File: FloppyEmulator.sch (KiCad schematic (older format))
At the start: 1 part

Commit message: Bit of update
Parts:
- added Q1: Crystal_GND24, symbol Crystal_GND24
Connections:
- net SPI2_MISO: no longer U?.52 (PC11/ADC1_EXTI11/ADC2_EXTI11/ADC3_EXTI11/I2S3_ext_SD/SDIO_D3/SPI3_MISO/UART4_RX/USART3_RX)
- net SPI2_MOSI: no longer U?.53 (PC12/I2S3_SD/SDIO_CK/SPI3_MOSI/UART5_TX/USART3_CK)
- net SPI2_SCK: no longer U?.51 (PC10/I2S3_CK/SDIO_D2/SPI3_SCK/UART4_TX/USART3_TX)
- net GND: now reaches U?.12 (VSSA)
- net GND: now also U?.18 (VSS), U?.63 (VSS)
- net +3V3: now reaches U?.13 (VDDA)
- net +3V3: now also U?.19 (VDD), U?.32 (VDD), U?.48 (VDD), U?.64 (VDD)
- net at U?.5 (PH0/RCC_OSC_IN): now also Q1.3
- net at U?.6 (PH1/RCC_OSC_OUT): now also Q1.1
- net SCL: now reaches U?.61 (CAN1_RX/I2C1_SCL/SDIO_D4/TIM10_CH1/TIM4_CH3/PB8)
- net SDA: now reaches U?.62 (CAN1_TX/DAC_EXTI9/I2C1_SDA/I2S2_WS/SDIO_D5/SPI2_NSS/TIM11_CH1/TIM4_CH4/PB9)
- new net SPI3_MISO: U?.52 (PC11/ADC1_EXTI11/ADC2_EXTI11/ADC3_EXTI11/I2S3_ext_SD/SDIO_D3/SPI3_MISO/UART4_RX/USART3_RX)
- new net SPI3_MOSI: U?.53 (PC12/I2S3_SD/SDIO_CK/SPI3_MOSI/UART5_TX/USART3_CK)
- new net SPI3_SCK: U?.51 (PC10/I2S3_CK/SDIO_D2/SPI3_SCK/UART4_TX/USART3_TX)
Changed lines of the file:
@@
 U 1 1 5A44968C
 P 8575 5200
-F 0 "U?" H 8575 3114 50  0000 C CNN
-F 1 "STM32F405RGTx" H 8575 3023 50  0000 C CNN
+F 0 "U?" H 8575 2925 50  0000 C CNN
+F 1 "STM32F405RGTx" H 8575 2800 50  0000 C CNN
 F 2 "LQFP64" H 12775 7075 50  0001 R TNN
 F 3 "" H 8575 5200 50  0001 C CNN
@@
 	12875 5100 13100 5100
 Text GLabel 4000 6300 0    50   Output ~ 0
-SPI2_SCK
+SPI3_SCK
 Text GLabel 4000 6400 0    50   Input ~ 0
-SPI2_MISO
+SPI3_MISO
 Text GLabel 4000 6500 0    50   Output ~ 0
-SPI2_MOSI
+SPI3_MOSI
 Wire Wire Line
 	4275 6300 4000 6300
@@
 Text Notes 5800 2625 0    60   ~ 0
 2 ??? Disk Change Detect on Shugart Interface or Density Select on IBM PC\n4 ???\n6 ??? Can be Drive Select 3 on Amiga\n8 <-- Index\n10 --> Motor Enable A\n12 --> Drive Select B\n14 --> Drive Select A\n16 --> Motor Enable B\n18 --> Step\n20 --> Dir\n22 --> Write Data\n24 --> Write Enable\n26 <-- Track 00\n28 <-- Write Protect\n30 <-- Read Data\n32 --> Side / Head\n34 <-- Disk Change / Ready
+$Comp
+L Crystal_GND24 Q1
+U 1 1 5A44A2C6
+P 3725 4850
+F 0 "Q1" V 3775 5425 50  0000 R CNN
+F 1 "Crystal_GND24" V 3700 5825 50  0000 R CNN
+F 2 "" H 3725 4850 50  0001 C CNN
+F 3 "" H 3725 4850 50  0001 C CNN
+	1    3725 4850
+	0    -1   -1   0
+$EndComp
+Wire Wire Line
+	3725 4700 3725 4550
+Wire Wire Line
+	3725 4550 4075 4550
+Wire Wire Line
+	4075 4550 4075 4800
+Wire Wire Line
+	4075 4800 4275 4800
+Wire Wire Line
+	4275 4900 4075 4900
+Wire Wire Line
+	4075 4900 4075 5125
+Wire Wire Line
+	4075 5125 3725 5125
+Wire Wire Line
+	3725 5125 3725 5000
+Text GLabel 1825 7825 0    60   Input ~ 0
++5VDC
+Text GLabel 1825 8125 0    60   Input ~ 0
+GND
+$Comp
+L GND #PWR?
+U 1 1 5A44A7FF
+P 1925 8275
+F 0 "#PWR?" H 1925 8025 50  0001 C CNN
+F 1 "GND" H 1930 8102 50  0001 C CNN
+F 2 "" H 1925 8275 50  0001 C CNN
+F 3 "" H 1925 8275 50  0001 C CNN
+	1    1925 8275
+	1    0    0    -1
+$EndComp
+Wire Wire Line
+	1925 8275 1925 8125
+Wire Wire Line
+	1925 8125 1825 8125
+Wire Wire Line
+	1825 7825 2100 7825
+$Comp
+L GND #PWR?
+U 1 1 5A44A98F
+P 8475 7200
+F 0 "#PWR?" H 8475 6950 50  0001 C CNN
+F 1 "GND" H 8480 7027 50  0001 C CNN
+F 2 "" H 8475 7200 50  0001 C CNN
+F 3 "" H 8475 7200 50  0001 C CNN
+	1    8475 7200
+	1    0    0    -1
+$EndComp
+$Comp
+L GND #PWR?
+U 1 1 5A44A9D8
+P 8575 7200
+F 0 "#PWR?" H 8575 6950 50  0001 C CNN
+F 1 "GND" H 8580 7027 50  0001 C CNN
+F 2 "" H 8575 7200 50  0001 C CNN
+F 3 "" H 8575 7200 50  0001 C CNN
+	1    8575 7200
+	1    0    0    -1
+$EndComp
+$Comp
+L GND #PWR?
+U 1 1 5A44A9E7
+P 8675 7200
+F 0 "#PWR?" H 8675 6950 50  0001 C CNN
+F 1 "GND" H 8680 7027 50  0001 C CNN
+F 2 "" H 8675 7200 50  0001 C CNN
+F 3 "" H 8675 7200 50  0001 C CNN
+	1    8675 7200
+	1    0    0    -1
+$EndComp
+Wire Wire Line
+	8375 3200 8375 3050
+Wire Wire Line
+	8375 3050 8775 3050
+Wire Wire Line
+	8775 3050 8775 3200
+Wire Wire Line
+	8675 3200 8675 3050
+Connection ~ 8675 3050
+Wire Wire Line
+	8575 2825 8575 3200
+Connection ~ 8575 3050
+Wire Wire Line
+	8475 3200 8475 3050
+Connection ~ 8475 3050
+Wire Wire Line
+	8575 2825 8750 2825
+Text GLabel 8750 2825 2    60   Input ~ 0
++3V3
+Wire Wire Line
+	12875 6100 13100 6100
+Wire Wire Line
+	12875 6200 13100 6200
+Text GLabel 13100 6100 2    50   Output ~ 0
+SCL
+Text GLabel 13100 6200 2    50   BiDi ~ 0
+SDA
 $EndSCHEMATC

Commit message: Signals assigned
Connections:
- net WRGATE: now reaches U?.10 (PC2/ADC1_IN12/ADC2_IN12/ADC3_IN12/I2S2_ext_SD/SPI2_MISO/USB_OTG_HS_ULPI_DIR)
- net WRDATA: now reaches U?.11 (PC3/ADC1_IN13/ADC2_IN13/ADC3_IN13/I2S2_SD/SPI2_MOSI/USB_OTG_HS_ULPI_NXT)
- net SEL0: now reaches U?.14 (ADC1_IN0/ADC2_IN0/ADC3_IN0/SYS_WKUP/TIM2_CH1/TIM2_ETR/TIM5_CH1/TIM8_ETR/UART4_TX/USART2_CTS/PA0)
- net SEL1: now reaches U?.15 (ADC1_IN1/ADC2_IN1/ADC3_IN1/TIM2_CH2/TIM5_CH2/UART4_RX/USART2_RTS/PA1)
- net SEL2: now reaches U?.16 (ADC1_IN2/ADC2_IN2/ADC3_IN2/TIM2_CH3/TIM5_CH3/TIM9_CH1/USART2_TX/PA2)
- net SEL3: now reaches U?.17 (ADC1_IN3/ADC2_IN3/ADC3_IN3/TIM2_CH4/TIM5_CH4/TIM9_CH2/USART2_RX/USB_OTG_HS_ULPI_D0/PA3)
- net INDEX: now reaches U?.2 (PC13/ANTI_TAMP/RTC_AF1)
- net TRACK0: now reaches U?.3 (PC14/RCC_OSC32_IN)
- net WPROT: now reaches U?.4 (PC15/ADC1_EXTI15/ADC2_EXTI15/ADC3_EXTI15/RCC_OSC32_OUT)
- net BEEP: now reaches U?.41 (I2C3_SCL/RCC_MCO_1/TIM1_CH1/USART1_CK/USB_OTG_FS_SOF/PA8)
- net LCD_DC: now reaches U?.54 (PD2/SDIO_CMD/TIM3_ETR/UART5_RX)
- net LCD_RESET: now reaches U?.55 (I2S3_CK/SPI1_SCK/SPI3_SCK/SYS_JTDO-SWO/TIM2_CH2/PB3)
- net BUTTON1: now reaches U?.56 (I2S3_ext_SD/SPI1_MISO/SPI3_MISO/SYS_JTRST/TIM3_CH1/PB4)
- net BUTTON2: now reaches U?.57 (CAN2_RX/I2C1_SMBA/I2S3_SD/SPI1_MOSI/SPI3_MOSI/TIM3_CH2/USB_OTG_HS_ULPI_D7/PB5)
- net BUTTON3: now reaches U?.58 (CAN2_TX/I2C1_SCL/TIM4_CH1/USART1_TX/PB6)
- net BUTTON4: now reaches U?.59 (I2C1_SDA/TIM4_CH2/USART1_RX/PB7)
- net SIDE: now reaches U?.8 (PC0/ADC1_IN10/ADC2_IN10/ADC3_IN10/USB_OTG_HS_ULPI_STP)
- net STEP: now reaches U?.9 (PC1/ADC1_IN11/ADC2_IN11/ADC3_IN11)
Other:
- note added: "BUTTONS, LED(s) and BEEPER"
- note added: "LCD"
- note added: "MFM Flow"
- note added: "OUTPUT SIGNALS:\n\n- Index\n- Track 0\n- Write Protect\n- Read Data\n- Disk Change/Ready\n- Reserved ???"
- note removed: "OUTPUT SIGNALS:\n\n- Index\n- Track 0\n- Write Protect\n- Read Data\n- Disk Change/Ready"
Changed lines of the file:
@@
 INPUT SIGNALS:\n\n- Drive Select 0\n- Drive Select 1\n- Motor Enable A\n- Motor Enable B\n- Dir\n- Side (INTERRUPT)\n- Step (INTERRUPT)\n- Write Gate (INTERRUPT)\n- Write Data (INTERRUPT)\n- Reserved ?
 Text Notes 3575 1650 0    60   ~ 0
-OUTPUT SIGNALS:\n\n- Index\n- Track 0\n- Write Protect\n- Read Data\n- Disk Change/Ready
+OUTPUT SIGNALS:\n\n- Index\n- Track 0\n- Write Protect\n- Read Data\n- Disk Change/Ready\n- Reserved ???
 Text Notes 1175 3025 0    60   ~ 0
 Amiga Drive ID readout:\n\n- turn Select off\n- turn Motor on and off\n- pulse Select and read ID bits on Ready line
@@
 	4275 4900 4075 4900
 Wire Wire Line
-	4075 4900 4075 5125
+	4075 4900 4075 5025
 Wire Wire Line
-	4075 5125 3725 5125
+	4075 5025 3725 5025
 Wire Wire Line
-	3725 5125 3725 5000
+	3725 5025 3725 5000
 Text GLabel 1825 7825 0    60   Input ~ 0
 +5VDC
@@
 Text GLabel 13100 6200 2    50   BiDi ~ 0
 SDA
+Text Notes 850  3825 0    60   ~ 0
+BUTTONS, LED(s) and BEEPER
+Text Notes 13700 6675 0    60   ~ 0
+MFM Flow
+Text Notes 3325 6450 0    60   ~ 0
+LCD
+Wire Wire Line
+	4275 5100 3125 5100
+Text Label 3125 5100 0    60   ~ 0
+LCD_DC
+Wire Wire Line
+	12875 5600 13650 5600
+Text Label 13650 5600 2    60   ~ 0
+LCD_RESET
+Wire Wire Line
+	12875 5700 13650 5700
+Wire Wire Line
+	12875 5800 13650 5800
+Wire Wire Line
+	12875 5900 13650 5900
+Wire Wire Line
+	12875 6000 13650 6000
+Text Label 13650 5700 2    60   ~ 0
+BUTTON1
+Text Label 13650 5800 2    60   ~ 0
+BUTTON2
+Text Label 13650 5900 2    60   ~ 0
+BUTTON3
+Text Label 13650 6000 2    60   ~ 0
+BUTTON4
+Wire Wire Line
+	4275 6600 2900 6600
+Wire Wire Line
+	4275 6700 2900 6700
+Wire Wire Line
+	4275 6800 2900 6800
+Text Label 2900 6600 0    60   ~ 0
+INDEX
+Text Label 2900 6700 0    60   ~ 0
+TRACK0
+Text Label 2900 6800 0    60   ~ 0
+WPROT
+Wire Wire Line
+	4275 5300 2900 5300
+Wire Wire Line
+	4275 5400 2900 5400
+Wire Wire Line
+	4275 5500 2900 5500
+Text Label 2900 5300 0    60   ~ 0
+SIDE
+Text Label 2900 5400 0    60   ~ 0
+STEP
+Text Label 2900 5500 0    60   ~ 0
+WRGATE
+Wire Wire Line
+	4275 5600 2900 5600
+Text Label 2900 5600 0    60   ~ 0
+WRDATA
+Wire Wire Line
+	12875 3600 13600 3600
+Wire Wire Line
+	12875 3700 13600 3700
+Wire Wire Line
+	12875 3800 13600 3800
+Wire Wire Line
+	12875 3900 13600 3900
+Text Label 13600 3600 2    60   ~ 0
+SEL0
+Text Label 13600 3700 2    60   ~ 0
+SEL1
+Text Label 13600 3800 2    60   ~ 0
+SEL2
+Text Label 13600 3900 2    60   ~ 0
+SEL3
+Wire Wire Line
+	12875 4400 13100 4400
+Text GLabel 13100 4400 2    50   Output ~ 0
+BEEP
 $EndSCHEMATC

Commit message: Draft components placement
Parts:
- added X1: Micro_SD_Card_Det, symbol Micro_SD_Card_Det
- added X2: Conn_01x09, components:QVGA_LCD_9pin, symbol Conn_01x09
- added X3: Conn_02x17_Odd_Even, Pin_Headers:Pin_Header_Straight_2x17_Pitch2.54mm, symbol Conn_02x17_Odd_Even
- added X4: Conn_01x04, Pin_Headers:Pin_Header_Angled_1x04_Pitch2.54mm, symbol Conn_01x04
- U1: renamed from U?; footprint LQFP64 -> Housings_QFP:LQFP-64_10x10mm_Pitch0.5mm
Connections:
- net +3V3: now also X2.1 (Pin_1)
- net GND: now also X1.11 (SHIELD), X1.6 (VSS), X1.9 (DET_B), X2.2 (Pin_2)
- net LCD_DC: now also X2.5 (Pin_5)
- net LCD_RESET: now also X2.4 (Pin_4)
- net SPI3_MISO: now also X2.9 (Pin_9)
- net SPI3_MOSI: now also X2.6 (Pin_6)
- net SPI3_NSS: now also X2.3 (Pin_3)
- net SPI3_SCK: now also X2.7 (Pin_7)
- new net BACKLIGHT: X2.8 (Pin_8)
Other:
- note added: "microSD connector:\nMOLEX 5027740891"
- note removed: "SD Card"

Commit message: Add microSD footprint. Update schematic and PCB
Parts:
- added U2, U3, U4, U5, U? (x2): SN74LVC2G07, TO_SOT_Packages_SMD:SOT-23-6, symbol SN74LVC2G07
- X1: footprint (none) -> components:MOLEX_5027740891
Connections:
- net labels added: CARD_DETECT, DIR
- wire segments 63 -> 113
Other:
- note added: "5-way SMD Joystick ALPS SKRHABE010"
- note added: "ESD?\nPull-ups?"
- note added: "MOLEX 5027740891"
- note added: "SN74LV1T34 Logic Buffer Translator\nSN74LVC2G07 Dual Open Drain Buffer"
- note added: "use open drain"
- note removed: "microSD connector:\nMOLEX 5027740891"
- moved on the sheet: X1, X3, X4

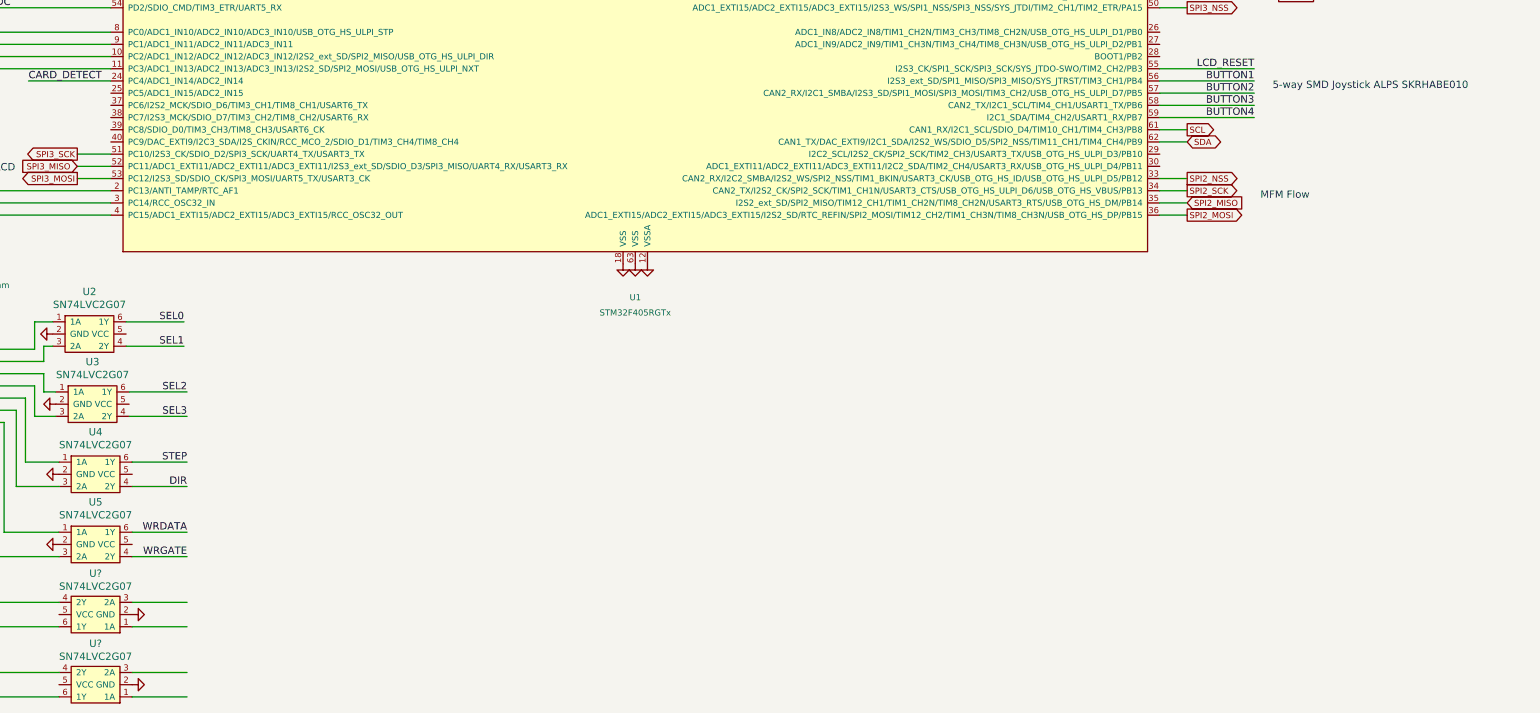
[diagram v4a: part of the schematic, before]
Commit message: Add ALPS 5-way joystick
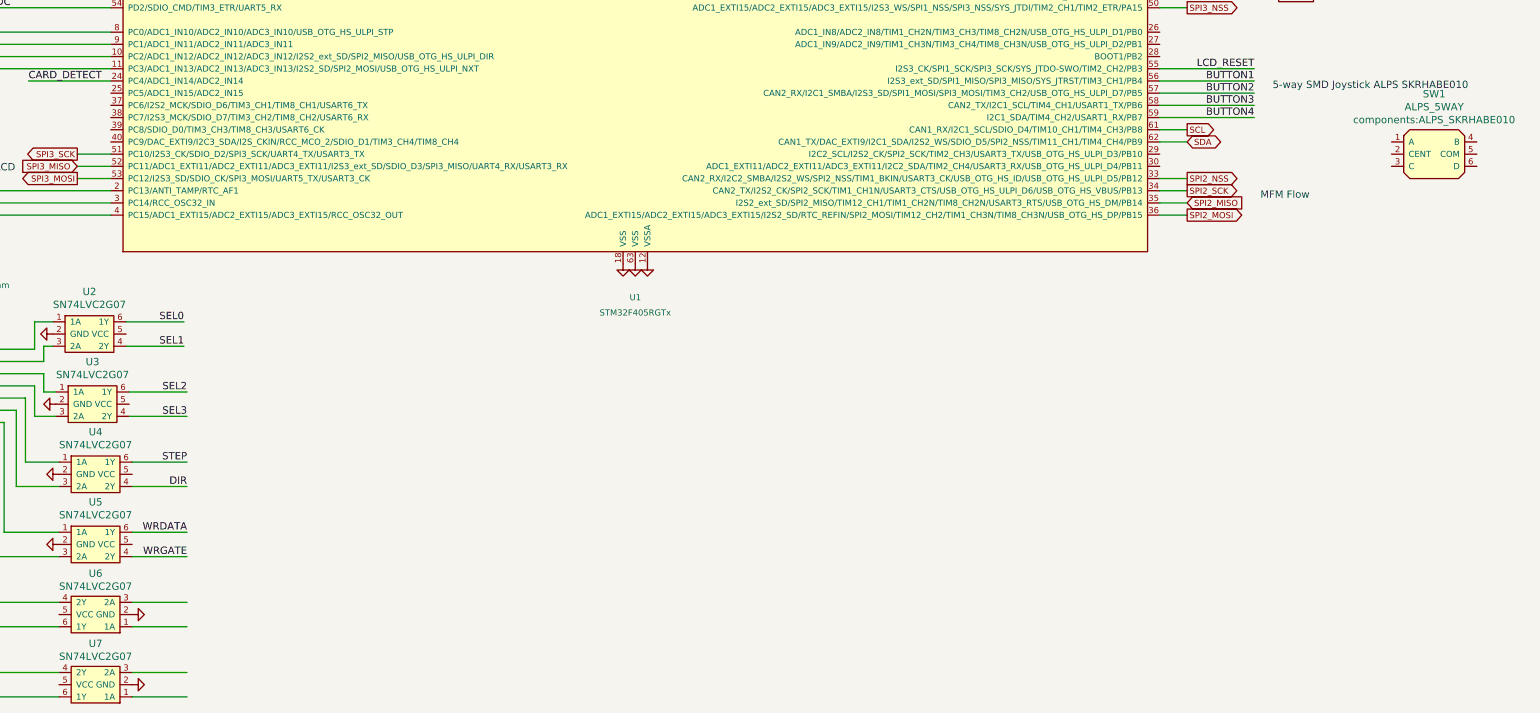
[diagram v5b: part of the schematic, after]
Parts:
- added SW1: ALPS_5WAY, components:ALPS_SKRHABE010, symbol ALPS_5WAY
- gave numbers to parts that had none: 2
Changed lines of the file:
@@
 WRDATA
 $Comp
-L SN74LVC2G07 U?
+L SN74LVC2G07 U6
 U 1 1 5A453572
 P 4150 10075
-F 0 "U?" H 4150 9738 60  0000 C CNN
+F 0 "U6" H 4150 9738 60  0000 C CNN
 F 1 "SN74LVC2G07" H 4150 9844 60  0000 C CNN
 F 2 "TO_SOT_Packages_SMD:SOT-23-6" H 4150 10325 60  0001 C CNN
@@
 $EndComp
 $Comp
-L SN74LVC2G07 U?
+L SN74LVC2G07 U7
 U 1 1 5A4535E1
 P 4150 10650
-F 0 "U?" H 4150 10313 60  0000 C CNN
+F 0 "U7" H 4150 10313 60  0000 C CNN
 F 1 "SN74LVC2G07" H 4150 10419 60  0000 C CNN
 F 2 "TO_SOT_Packages_SMD:SOT-23-6" H 4150 10900 60  0001 C CNN
@@
 	2900 10750 3850 10750
 $Comp
-L GND #PWR?
+L GND #PWR013
 U 1 1 5A4538FF
 P 4450 10075
-F 0 "#PWR?" H 4450 9825 50  0001 C CNN
+F 0 "#PWR013" H 4450 9825 50  0001 C CNN
 F 1 "GND" H 4455 9902 50  0001 C CNN
 F 2 "" H 4450 10075 50  0001 C CNN
@@
 $EndComp
 $Comp
-L GND #PWR?
+L GND #PWR014
 U 1 1 5A45393A
 P 4450 10650
-F 0 "#PWR?" H 4450 10400 50  0001 C CNN
+F 0 "#PWR014" H 4450 10400 50  0001 C CNN
 F 1 "GND" H 4455 10477 50  0001 C CNN
 F 2 "" H 4450 10650 50  0001 C CNN
@@
 Text Notes 13800 5775 0    60   ~ 0
 5-way SMD Joystick ALPS SKRHABE010
+$Comp
+L ALPS_5WAY SW1
+U 1 1 5A4545D4
+P 15125 6300
+F 0 "SW1" H 15125 6793 60  0000 C CNN
+F 1 "ALPS_5WAY" H 15125 6687 60  0000 C CNN
+F 2 "components:ALPS_SKRHABE010" H 15125 6581 60  0000 C CNN
+F 3 "" H 15125 6300 60  0001 C CNN
+	1    15125 6300
+	1    0    0    -1
+$EndComp
 $EndSCHEMATC

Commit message: Up
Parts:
- added U8, U9: SN74LVC2G07, TO_SOT_Packages_SMD:SOT-23-6, symbol FloppyEmulator:SN74LVC2G07
- Q1: symbol Crystal_GND24 -> device1:Crystal_GND24
- SW1: symbol ALPS_5WAY -> FloppyEmulator:ALPS_5WAY
- U1: symbol STM32F405RGTx -> FloppyEmulator-rescue:STM32F405RGTx-RESCUE-FloppyEmulator
- U2, U3, U4, U5, U6, U7: symbol SN74LVC2G07 -> FloppyEmulator:SN74LVC2G07
- X1: symbol Micro_SD_Card_Det -> FloppyEmulator-rescue:Micro_SD_Card_Det-RESCUE-FloppyEmulator
- X2: symbol Conn_01x09 -> FloppyEmulator-rescue:Conn_01x09-RESCUE-FloppyEmulator
- X3: symbol Conn_02x17_Odd_Even -> FloppyEmulator-rescue:Conn_02x17_Odd_Even-RESCUE-FloppyEmulator
- X4: symbol Conn_01x04 -> FloppyEmulator-rescue:Conn_01x04-RESCUE-FloppyEmulator
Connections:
- net labels added: OSC_IN, OSC_OUT, RDY
- wire segments 113 -> 141
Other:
- moved on the sheet: U2, U3

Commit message: Layout and schematic update
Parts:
- added C1, C2, C3, C4, C5: 0,1, Capacitors_SMD:C_0603, symbol device1:C
- added Q2: BC817, TO_SOT_Packages_SMD:SOT-23, symbol device1:Q_NPN_BEC
- added R1: 10K, Resistors_SMD:R_0603, symbol device1:R
- added X5: SWD, Pin_Headers:Pin_Header_Angled_1x04_Pitch2.54mm, symbol FloppyEmulator-rescue:Conn_01x04-RESCUE-FloppyEmulator
- X4: value Conn_01x04 -> TE 171826-4; footprint Pin_Headers:Pin_Header_Angled_1x04_Pitch2.54mm -> components:171826-4
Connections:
- net labels added: BOOT0, BUTTON5, LED1, NRST, VBAT, VCAP1, VCAP2
- wire segments 141 -> 208
- no-connect marks 0 -> 2

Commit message: Caps added. PCB update
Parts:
- added C10, C11, C12, C13, C14, C15, C16, C17, C18, C8, C9: 0,1, Capacitors_SMD:C_0603, symbol device1:C
- added C6, C7: 2u2, Capacitors_SMD:C_0805, symbol device1:C
- added U10: AP1117-15, TO_SOT_Packages_SMD:SOT-223-3_TabPin2, symbol regul1:AP1117-15
- Q1: footprint (none) -> Crystals:Crystal_SMD_HC49-SD; symbol device1:Crystal_GND24 -> device1:Crystal
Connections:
- wire segments 208 -> 261
